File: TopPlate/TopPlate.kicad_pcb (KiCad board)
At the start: 2 copper layers, 135.3 x 94.8 mm, 5 parts

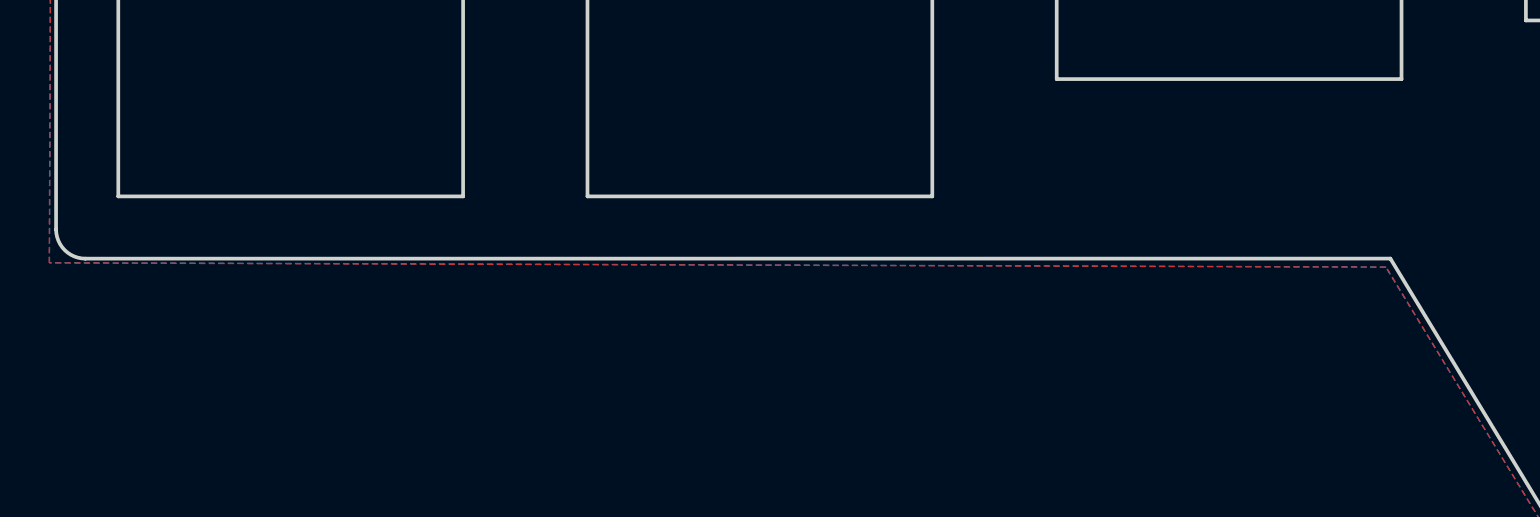
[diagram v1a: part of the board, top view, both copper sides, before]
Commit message: Fix top/bottom plates edges
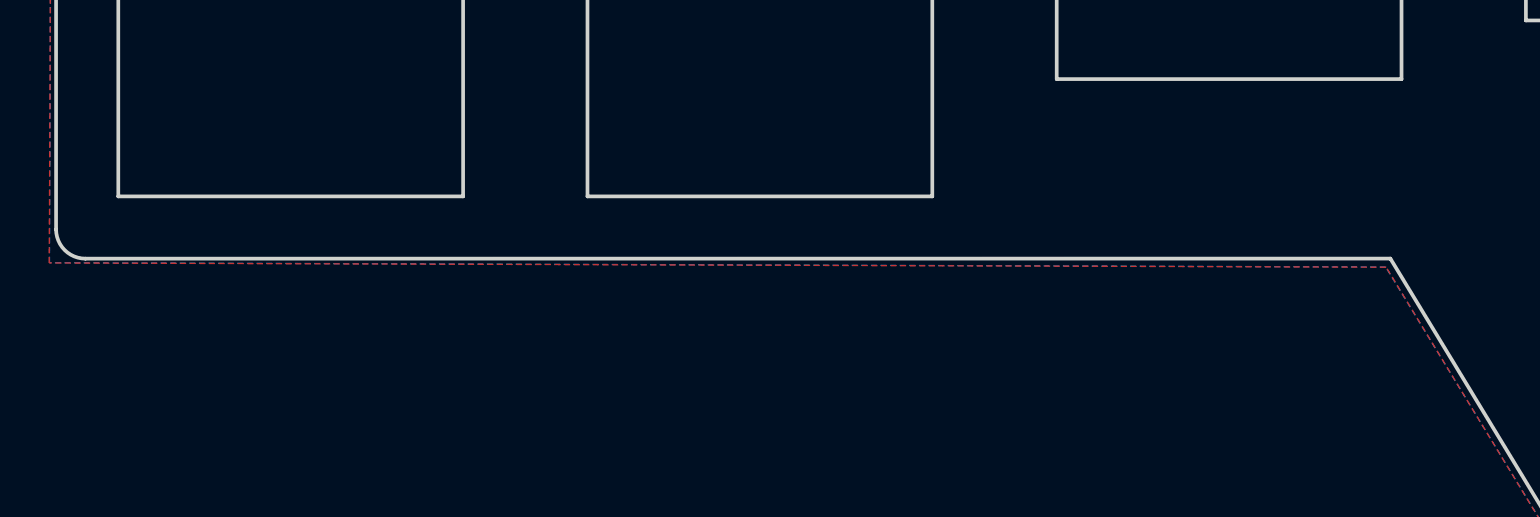
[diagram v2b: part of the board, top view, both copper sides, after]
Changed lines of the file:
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@@
     (0 F.Cu signal)
     (31 B.Cu signal)
-    (32 B.Adhes user hide)
-    (33 F.Adhes user hide)
-    (34 B.Paste user hide)
-    (35 F.Paste user hide)
-    (36 B.SilkS user hide)
-    (37 F.SilkS user hide)
-    (38 B.Mask user hide)
-    (39 F.Mask user hide)
-    (40 Dwgs.User user hide)
-    (41 Cmts.User user hide)
-    (42 Eco1.User user hide)
+    (32 B.Adhes user)
+    (33 F.Adhes user)
+    (34 B.Paste user)
+    (35 F.Paste user)
+    (36 B.SilkS user)
+    (37 F.SilkS user)
+    (38 B.Mask user)
+    (39 F.Mask user)
+    (40 Dwgs.User user)
+    (41 Cmts.User user)
+    (42 Eco1.User user)
     (43 Eco2.User user)
     (44 Edge.Cuts user)
     (45 Margin user)
-    (46 B.CrtYd user hide)
+    (46 B.CrtYd user)
     (47 F.CrtYd user)
-    (48 B.Fab user hide)
-    (49 F.Fab user hide)
+    (48 B.Fab user)
+    (49 F.Fab user)
   )
   (setup
@@
   (gr_line (start 197.11378 64.72553) (end 203.066905 64.72553) (angle 90) (layer Edge.Cuts) (width 0.15))
   (gr_line (start 204.25753 65.916155) (end 204.25753 114.136468) (angle 90) (layer Edge.Cuts) (width 0.15))
-  (gr_line (start 91.14378 124.25928) (end 144.130968 124.25678) (angle 90) (layer Edge.Cuts) (width 0.15))
+  (gr_line (start 91.146905 124.25928) (end 144.130968 124.25678) (angle 90) (layer Edge.Cuts) (width 0.15))
   (gr_line (start 154.25128 140.92553) (end 192.35128 145.68803) (angle 90) (layer Edge.Cuts) (width 0.15))
   (gr_line (start 154.25128 140.92553) (end 144.130968 124.25678) (angle 90) (layer Edge.Cuts) (width 0.15))
